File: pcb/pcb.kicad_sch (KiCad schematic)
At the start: 82 parts, among them J1 MJ-4PP-9, SW1 KEY_SW, SW10 KEY_SW, SW11 KEY_SW, SW12 KEY_SW, SW13 KEY_SW, SW14 KEY_SW, SW15 KEY_SW, SW16 KEY_SW, SW17 KEY_SW, SW18 KEY_SW, SW19 KEY_SW, SW2 KEY_SW, SW20 KEY_SW, SW21 KEY_SW, SW22 KEY_SW, SW23 KEY_SW, SW24 KEY_SW, SW25 KEY_SW, SW26 KEY_SW, SW27 RotaryEncoder, SW3 KEY_SW, SW30 KEY_SW, SW31 KEY_SW, SW32 KEY_SW, SW33 KEY_SW, SW34 KEY_SW, SW35 KEY_SW, SW36 KEY_SW, SW37 KEY_SW, SW38 KEY_SW, SW39 KEY_SW, SW4 KEY_SW, SW40 KEY_SW, SW41 KEY_SW, SW42 KEY_SW, SW43 KEY_SW, SW44 KEY_SW, SW45 KEY_SW, SW46 KEY_SW, SW47 KEY_SW, SW48 KEY_SW, SW49 KEY_SW, SW5 KEY_SW, SW50 KEY_SW, SW51 KEY_SW, SW52 KEY_SW, SW53 KEY_SW, SW54 KEY_SW, SW55 RotaryEncoder, SW6 KEY_SW, SW60 RESET_SW, SW7 KEY_SW, SW8 KEY_SW, SW9 KEY_SW

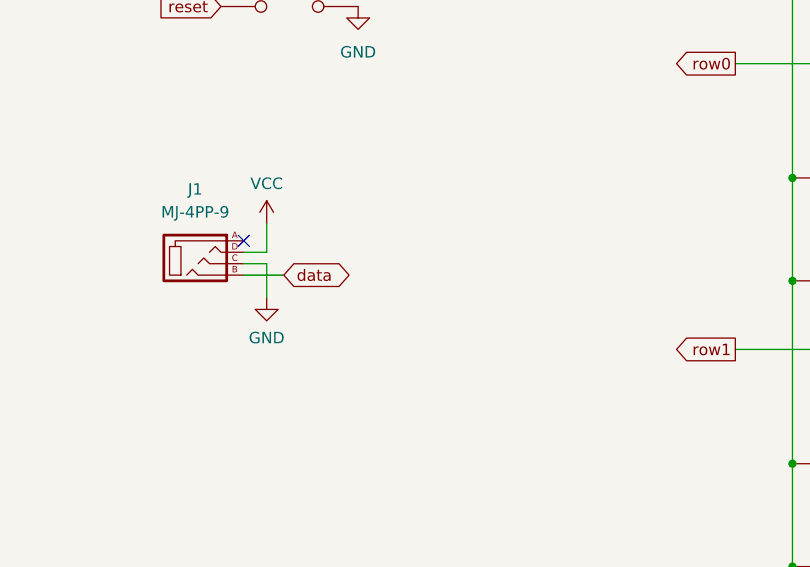
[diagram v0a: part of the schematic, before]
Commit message: link fotprint
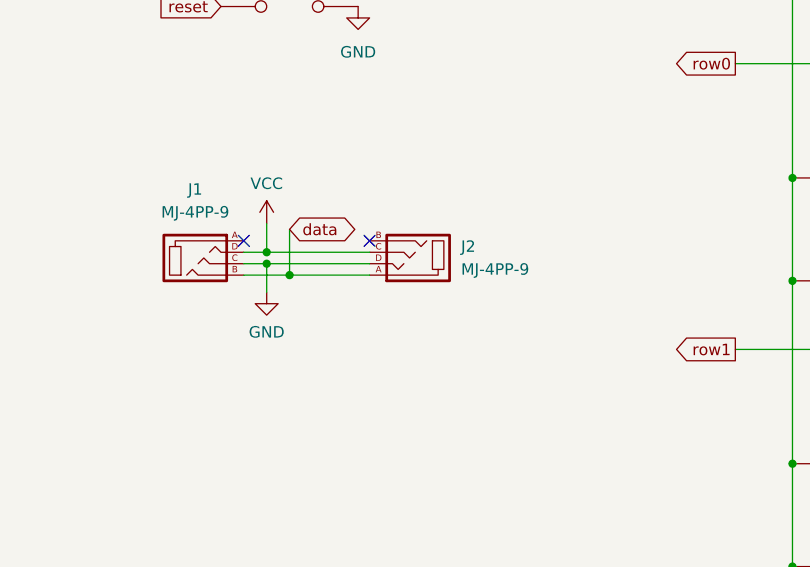
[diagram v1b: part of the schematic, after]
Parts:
- added J2: MJ-4PP-9, kbd:MJ-4PP-9, symbol kbd:MJ-4PP-9
- D1, D10, D11, D12, D13, D14, D15, D16, D17, D18, D19, D2, D20, D21, D22, D23, D24, D25, D26, D27, D3, D4, D5, D6, D7, D8, D9: footprint (none) -> keebio:Diode-dual
- J1: footprint (none) -> kbd:MJ-4PP-9
- SW1, SW10, SW11, SW12, SW13, SW14, SW15, SW16, SW17, SW18, SW19, SW2, SW20, SW21, SW22, SW23, SW24, SW25, SW26, SW3, SW31, SW32, SW33, SW34, SW35, SW36, SW37, SW38, SW39, SW4, SW40, SW41, SW42, SW43, SW44, SW45, SW46, SW47, SW48, SW49, SW5, SW50, SW51, SW52, SW53, SW54, SW6, SW7, SW8, SW9: footprint (none) -> kbd:keyswitch_cherrymx_hotswap_1u
- SW27, SW30, SW55: footprint (none) -> keebio:RotaryEncoder_EC11
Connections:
- net GND: now also J2.D
- net VCC: now also J2.C
- net data: now also J2.A
- no-connect marks 1 -> 2

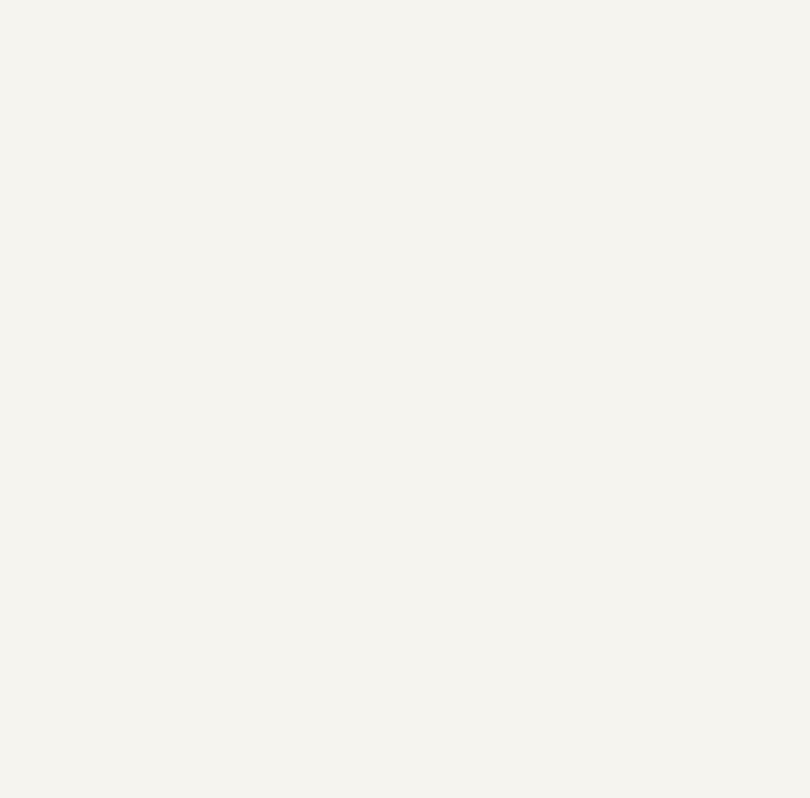
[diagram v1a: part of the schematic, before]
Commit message: ESP32-S3-WROOM-1
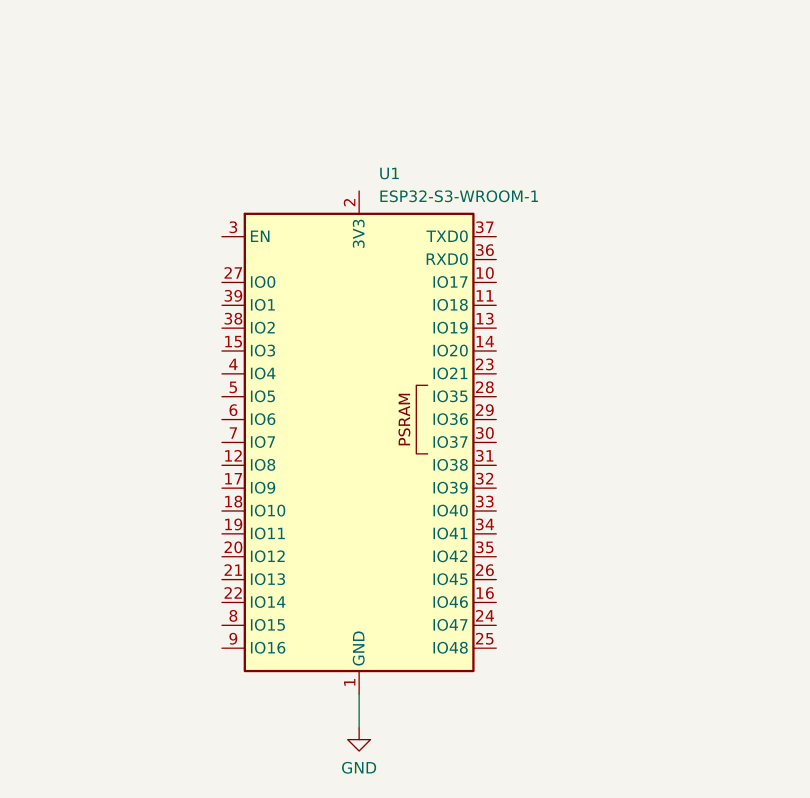
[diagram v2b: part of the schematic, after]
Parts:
- added U1: ESP32-S3-WROOM-1, RF_Module:ESP32-S3-WROOM-1, symbol RF_Module:ESP32-S3-WROOM-1
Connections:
- net GND: now also U1.1 (GND), U1.40 (GND), U1.41 (GND)
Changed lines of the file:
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@@
 (kicad_sch (version 20230121) (generator eeschema)
-  (paper "A4")
+  (paper "A3")
   (junction (at 234.95 25.4) (diameter 0) (color 0 0 0 0)
   )
@@
   )
   (wire (pts (xy 260.35 100.33) (xy 260.35 120.65))
+    (stroke (width 0) (type default))
+  )
+  (wire (pts (xy 127 244.475) (xy 127 240.665))
     (stroke (width 0) (type default))
   )
@@
     )
   )
+  (symbol (lib_id "RF_Module:ESP32-S3-WROOM-1") (at 127 212.725 0) (unit 1)
+    (in_bom yes) (on_board yes) (dnp no) (fields_autoplaced)
+    (property "Reference" "U1" (at 129.1941 182.88 0)
+      (effects (font (size 1.27 1.27)) (justify left))
+    )
+    (property "Value" "ESP32-S3-WROOM-1" (at 129.1941 185.42 0)
+      (effects (font (size 1.27 1.27)) (justify left))
+    )
+    (property "Footprint" "RF_Module:ESP32-S3-WROOM-1" (at 127 210.185 0)
+      (effects (font (size 1.27 1.27)) hide)
+    )
+    (property "Datasheet" "https://www.espressif.com/sites/default/files/documentation/esp32-s3-wroom-1_wroom-1u_datasheet_en.pdf" (at 127 212.725 0)
+      (effects (font (size 1.27 1.27)) hide)
+    )
+    (pin "23")
+    (pin "17")
+    (pin "4")
+    (pin "2")
+    (pin "35")
+    (pin "20")
+    (pin "19")
+    (pin "38")
+    (pin "5")
+    (pin "15")
+    (pin "26")
+    (pin "1")
+    (pin "29")
+    (pin "39")
+    (pin "8")
+    (pin "22")
+    (pin "11")
+    (pin "24")
+    (pin "7")
+    (pin "41")
+    (pin "32")
+    (pin "25")
+    (pin "27")
+    (pin "9")
+    (pin "30")
+    (pin "16")
+    (pin "33")
+    (pin "3")
+    (pin "36")
+    (pin "6")
+    (pin "18")
+    (pin "37")
+    (pin "28")
+    (pin "10")
+    (pin "13")
+    (pin "40")
+    (pin "34")
+    (pin "21")
+    (pin "14")
+    (pin "31")
+    (pin "12")
+    (instances
+      (project "pcb"
+        (path "/ca1682eb-af97-4baf-a70b-d30c3b256c66"
+          (reference "U1") (unit 1)
+        )
+      )
+    )
+  )
   (symbol (lib_id "kbd:SW_PUSH") (at 191.77 120.65 0) (unit 1)
     (in_bom yes) (on_board yes) (dnp no) (fields_autoplaced)
@@
         )
       )
+    )
+  )
+  (symbol (lib_id "power:GND") (at 127 244.475 0) (unit 1)
+    (in_bom yes) (on_board yes) (dnp no) (fields_autoplaced)
+    (property "Reference" "#PWR07" (at 127 250.825 0)
+      (effects (font (size 1.27 1.27)) hide)
+    )
+    (property "Value" "GND" (at 127 248.92 0)
+      (effects (font (size 1.27 1.27)))
+    )
+    (property "Footprint" "" (at 127 244.475 0)
+      (effects (font (size 1.27 1.27)) hide)
+    )
+    (property "Datasheet" "" (at 127 244.475 0)
+      (effects (font (size 1.27 1.27)) hide)
+    )
+    (pin "1")
+    (instances
+      (project "pcb"
+        (path "/ca1682eb-af97-4baf-a70b-d30c3b256c66"
+          (reference "#PWR07") (unit 1)
+        )
+      )

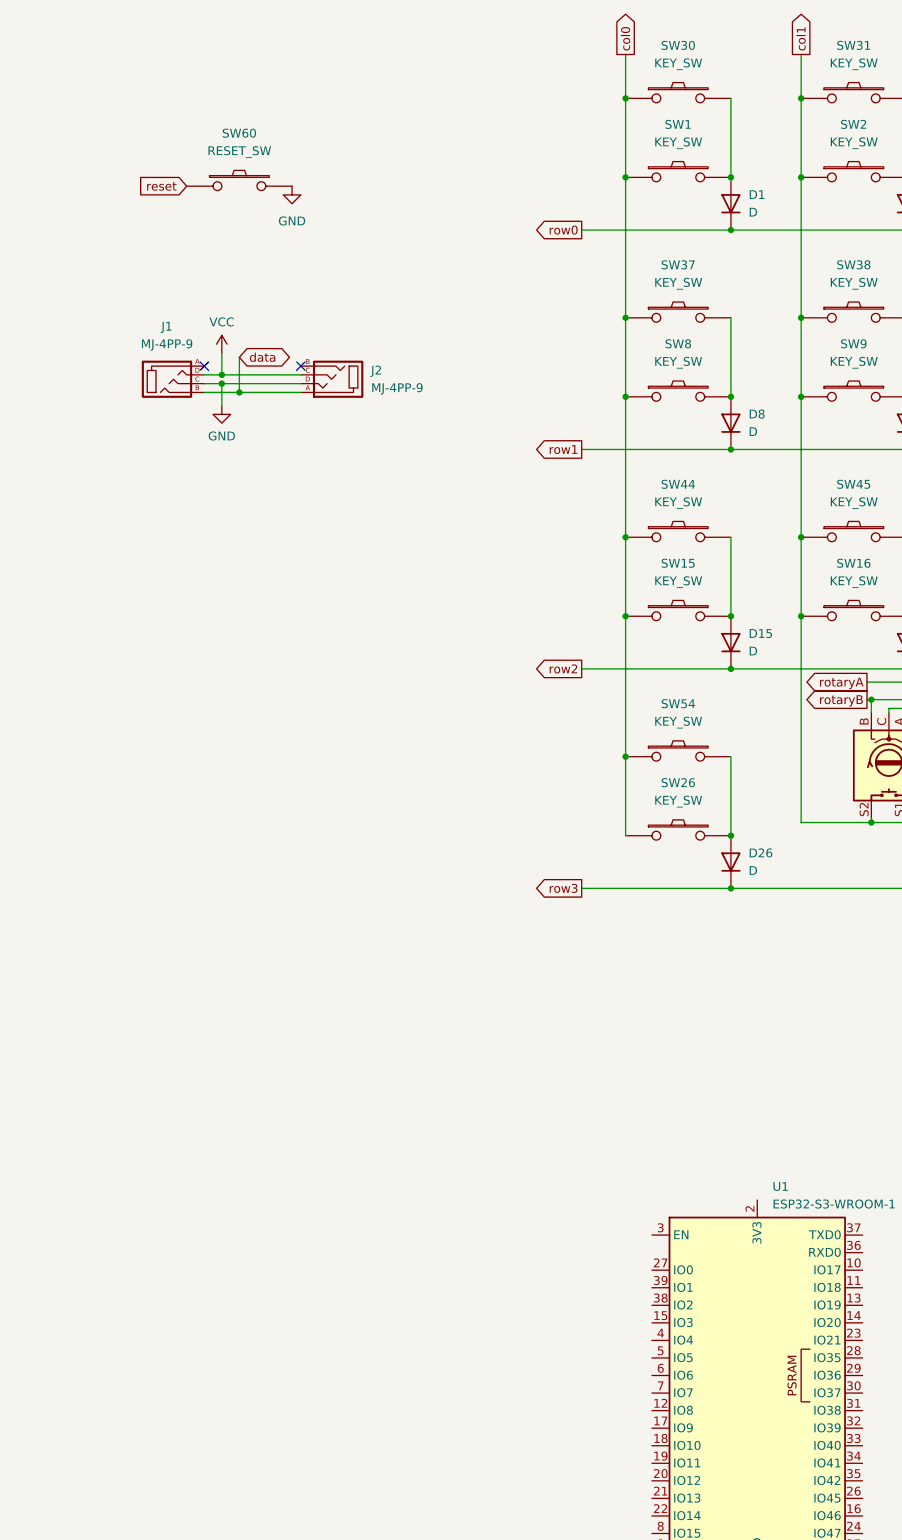
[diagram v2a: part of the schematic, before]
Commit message: Boot Mode close #6
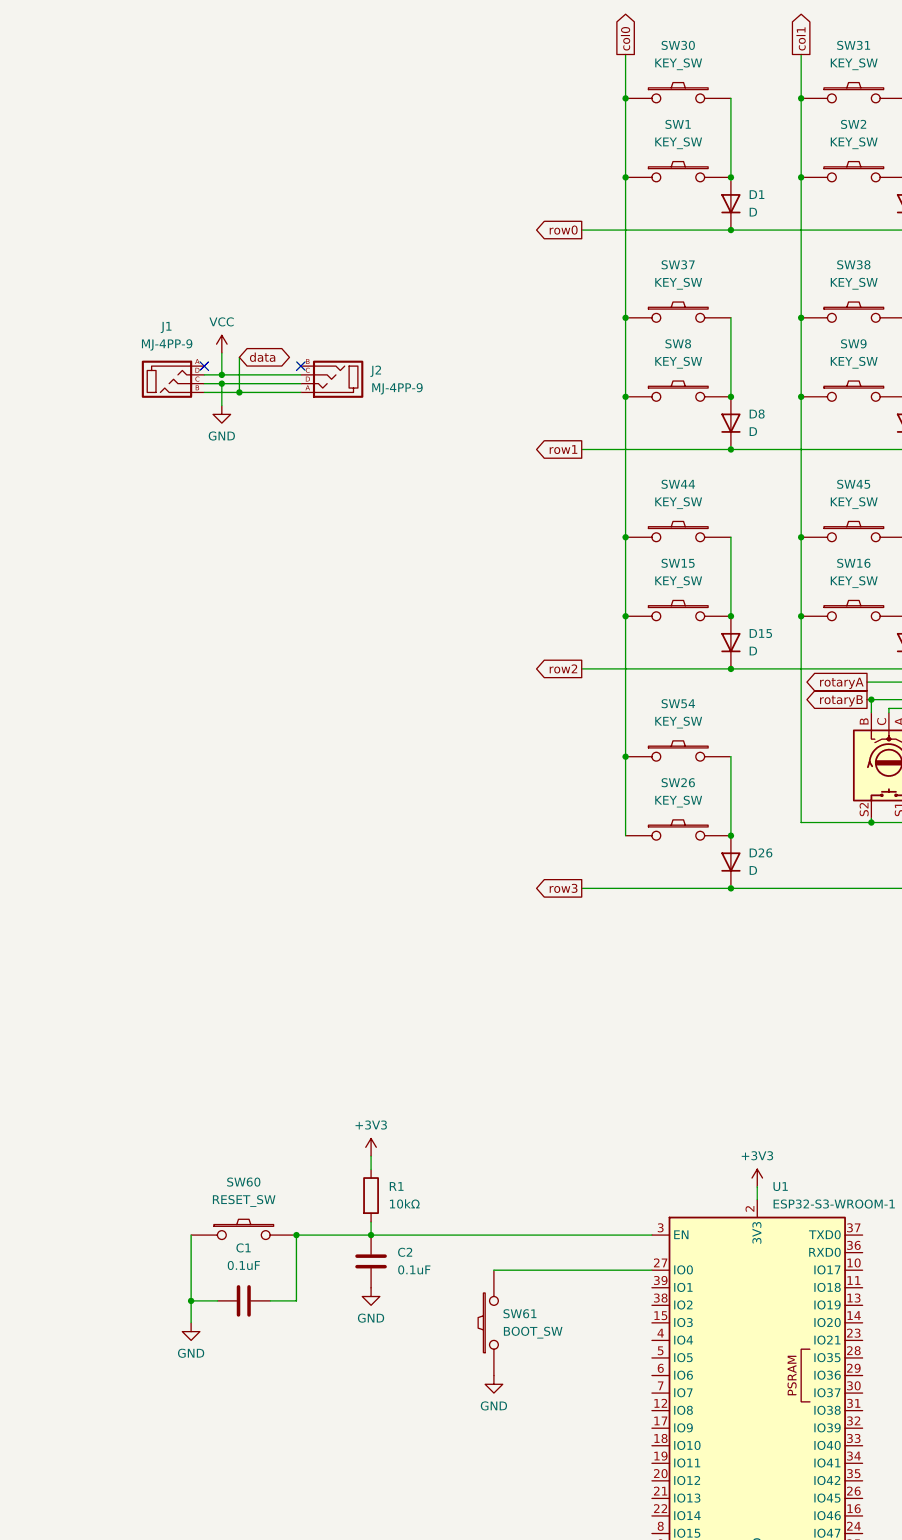
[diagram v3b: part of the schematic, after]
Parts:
- added C1, C2: 0.1uF, symbol Device:C
- added R1: 10kΩ, symbol Device:R
- added SW61: BOOT_SW, symbol kbd:SW_PUSH
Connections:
- net reset is gone; now on net GND: SW60.1
- net GND: now also C1.1, C2.1, SW61.1; no longer SW60.2
- net +3V3: now reaches U1.2 (3V3)
- net +3V3: now also R1.1
- net at U1.27 (IO0): now also SW61.2
- net at U1.3 (EN): now also SW60.2, C1.2, C2.2, R1.2
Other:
- moved on the sheet: SW60

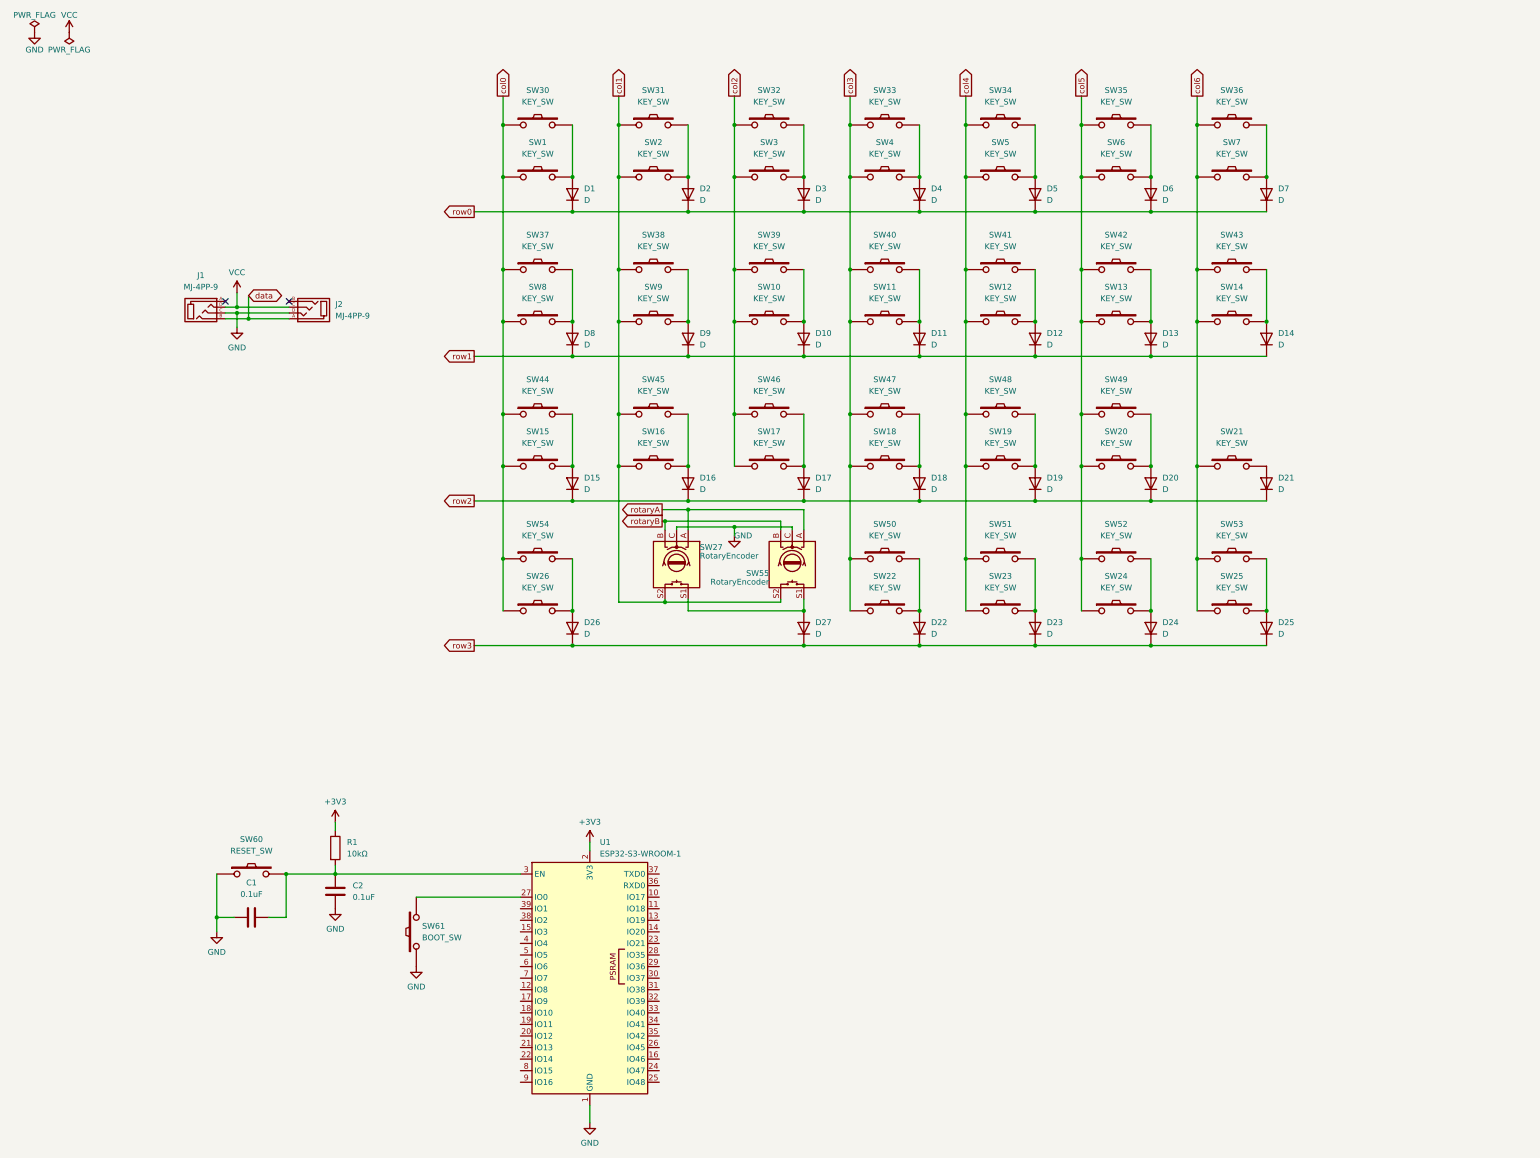
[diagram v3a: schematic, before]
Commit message: USB type-C close #7
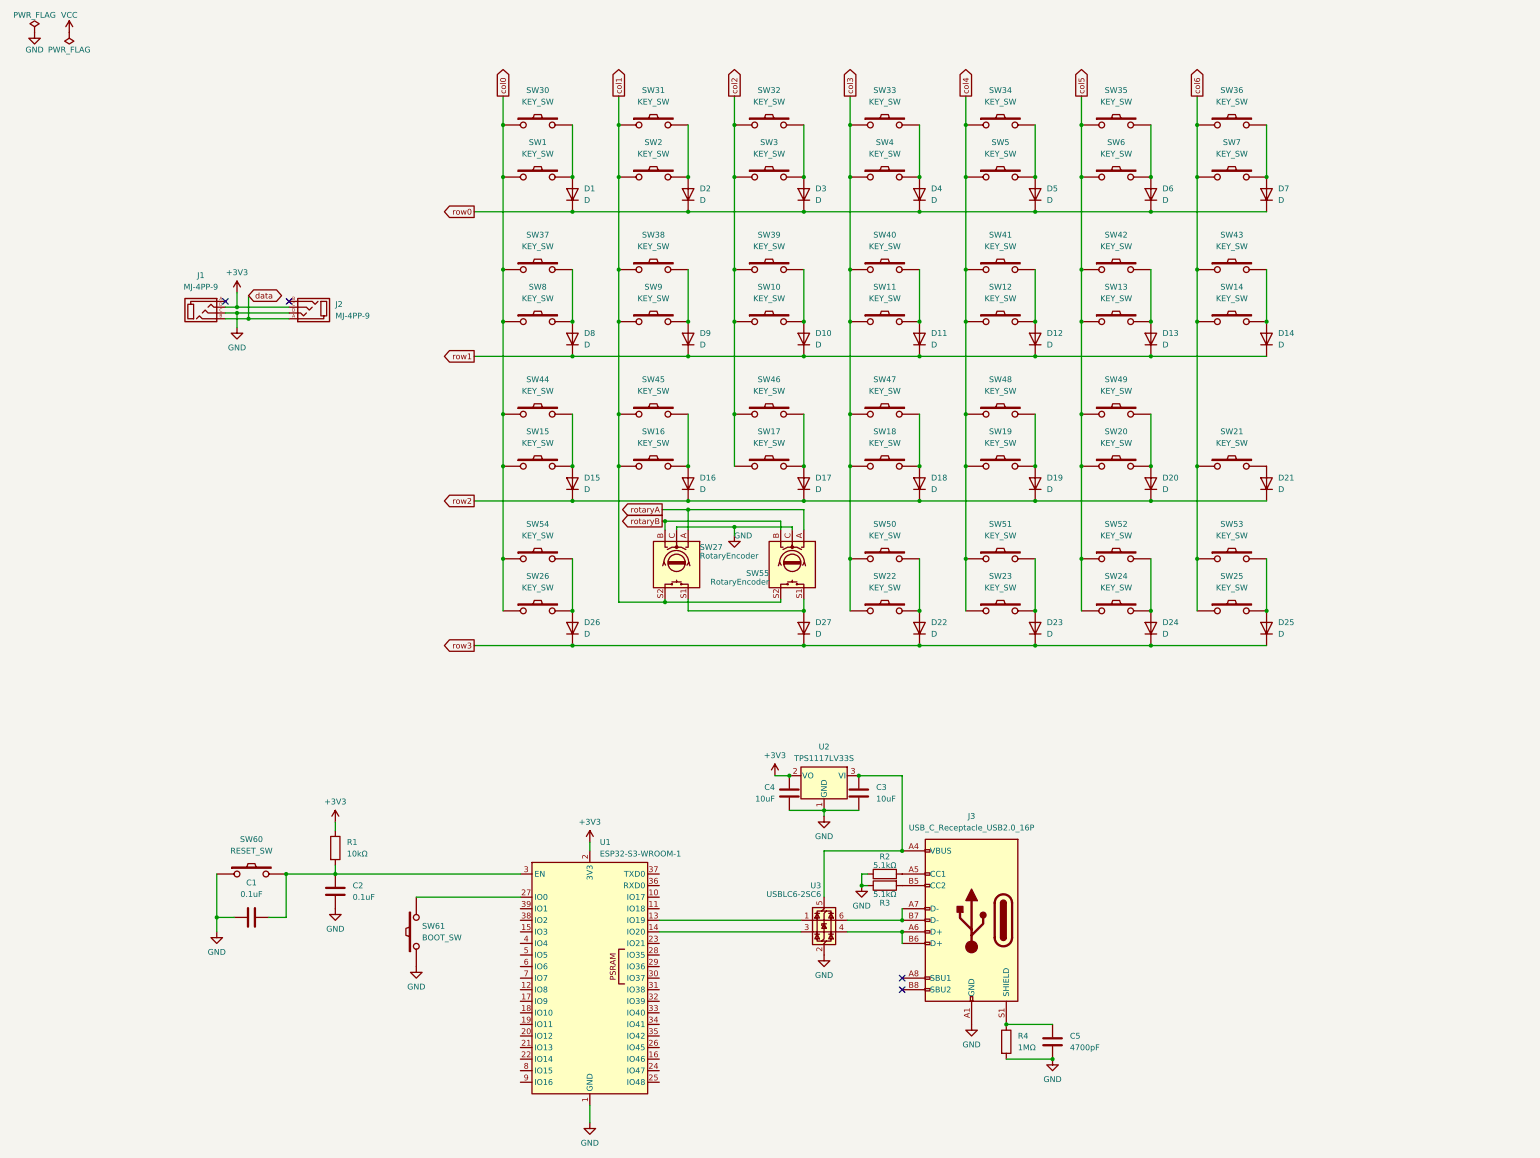
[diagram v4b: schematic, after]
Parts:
- added C3, C4: 10uF, symbol Device:C
- added C5: 4700pF, symbol Device:C
- added J3: USB_C_Receptacle_USB2.0_16P, symbol Connector:USB_C_Receptacle_USB2.0_16P
- added R2, R3: 5.1kΩ, symbol Device:R
- added R4: 1MΩ, symbol Device:R
- added U2: TPS1117LV33S, symbol lib:TPS1117LV33S
- added U3: USBLC6-2SC6, Package_TO_SOT_SMD:SOT-23-6, symbol Power_Protection:USBLC6-2SC6
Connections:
- net +3V3: now also J1.D, J2.C, C4.1, U2.2 (VO)
- net GND: now also C3.2, C4.2, C5.2, J3.A1 (GND), J3.A12 (GND), J3.B1 (GND), J3.B12 (GND), R2.1, R3.1, R4.2, U2.1 (GND), U3.2 (GND)
- net VCC: no longer J1.D, J2.C
- net at U1.13 (IO19): now also U3.1 (I/O1)
- net at U1.14 (IO20): now also U3.3 (I/O2)
- new net: C5.1, J3.S1 (SHIELD), R4.1
- new net: J3.A6 (D+), J3.B6 (D+), U3.4 (I/O2)
- new net: C3.1, J3.A4 (VBUS), J3.A9 (VBUS), J3.B4 (VBUS), J3.B9 (VBUS), U2.3 (VI), U3.5 (VBUS)
- new net: J3.A7 (D-), J3.B7 (D-), U3.6 (I/O1)
- new net: J3.A5 (CC1), R2.2
- new net: J3.B5 (CC2), R3.2
- no-connect marks 2 -> 4
